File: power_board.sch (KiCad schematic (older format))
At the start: 25 parts, among them CON1 MICROUSB, J3 Conn_02x03_Odd_Even, J31 Conn_01x01, J32 Conn_01x01, J33 Conn_01x01, J34 Conn_01x01, SW1 SW_Push, U2 FT232RL, U4 ATMEGA328P-AU, U8 PCA9555PW, U9 PCA9555PW, Y1 Crystal

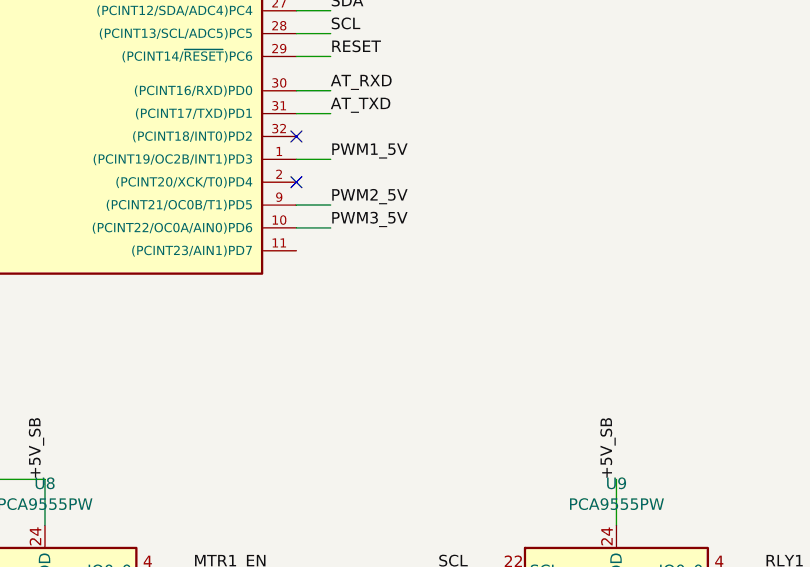
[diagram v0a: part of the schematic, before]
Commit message: Motor control positioning
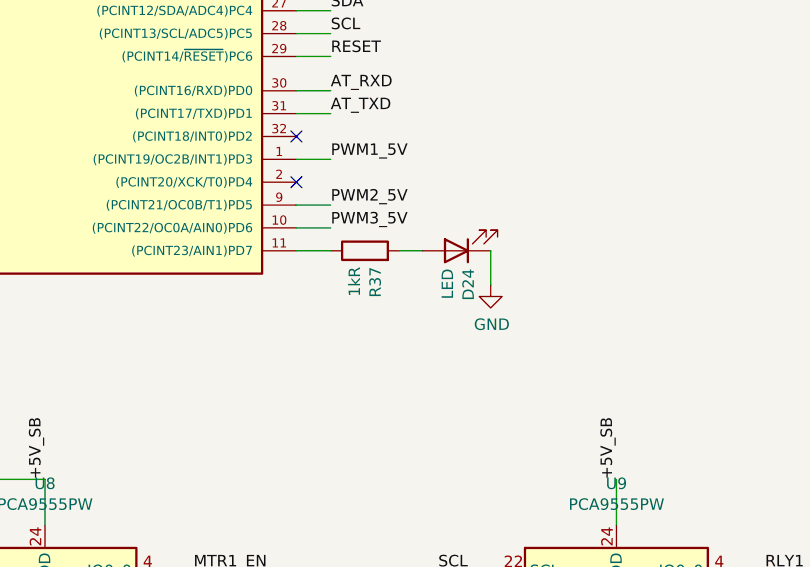
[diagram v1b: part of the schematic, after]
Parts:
- added D24: LED, lsts-discretes:LED_0603, symbol Device:LED
- added R37: 1kR, lsts-passives:R_0603, symbol Device:R
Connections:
- net GND: now also D24.1 (K)
- net at U4.11 ((PCINT23/AIN1)PD7): now also R37.1
- new net: D24.2 (A), R37.2
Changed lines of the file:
@@
 Text Label 3000 1500 0    50   ~ 0
 PWR_CTR
+$Comp
+L Device:LED D24
+U 1 1 5E321428
+P 3550 3800
+F 0 "D24" V 3497 3878 50  0000 L CNN
+F 1 "LED" V 3588 3878 50  0000 L CNN
+F 2 "lsts-discretes:LED_0603" H 3550 3800 50  0001 C CNN
+F 3 "~" H 3550 3800 50  0001 C CNN
+	1    3550 3800
+	-1   0    0    1
+$EndComp
+Wire Wire Line
+	3400 3800 3300 3800
+$Comp
+L Device:R R37
+U 1 1 5E32142F
+P 3150 3800
+F 0 "R37" H 3080 3754 50  0000 R CNN
+F 1 "1kR" H 3080 3845 50  0000 R CNN
+F 2 "lsts-passives:R_0603" V 3080 3800 50  0001 C CNN
+F 3 "~" H 3150 3800 50  0001 C CNN
+	1    3150 3800
+	0    -1   -1   0
+$EndComp
+Wire Wire Line
+	2850 3800 3000 3800
+$Comp
+L power:GND #PWR040
+U 1 1 5E35F179
+P 3700 3950
+F 0 "#PWR040" H 3700 3700 50  0001 C CNN
+F 1 "GND" H 3705 3777 50  0000 C CNN
+F 2 "" H 3700 3950 50  0001 C CNN
+F 3 "" H 3700 3950 50  0001 C CNN
+	1    3700 3950
+	1    0    0    -1
+$EndComp
+Wire Wire Line
+	3700 3800 3700 3950
 $EndSCHEMATC

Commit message: Motor control finished
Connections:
- net MTR6_BW: now also U9.6 (IO0_2)
- net MTR6_EN: now also U9.4 (IO0_0)
- net MTR6_FW: now also U9.5 (IO0_1)
- net MTR7_BW: now also U9.9 (IO0_5)
- net MTR7_EN: now also U9.7 (IO0_3)
- net MTR7_FW: now also U9.8 (IO0_4)
- net MTR8_BW: now also U9.13 (IO1_0)
- net MTR8_EN: now also U9.10 (IO0_6)
- net MTR8_FW: now also U9.11 (IO0_7)
- net RLY1_EN: now also U9.14 (IO1_1); no longer U9.4 (IO0_0)
- net RLY2_EN: now also U9.15 (IO1_2); no longer U9.5 (IO0_1)
- net RLY3_EN: now also U9.16 (IO1_3); no longer U9.6 (IO0_2)
- net RLY4_EN: now also U9.17 (IO1_4); no longer U9.7 (IO0_3)
- net RLY5_EN: now also U9.18 (IO1_5); no longer U9.8 (IO0_4)
- no-connect marks 34 -> 25
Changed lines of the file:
@@
 	2250 6700 2400 6700
 Wire Wire Line
-	4750 5200 4900 5200
-Wire Wire Line
-	4750 5300 4900 5300
-Wire Wire Line
-	4750 5400 4900 5400
-Wire Wire Line
-	4750 5500 4900 5500
-Wire Wire Line
-	4750 5600 4900 5600
+	4750 6200 4900 6200
+Wire Wire Line
+	4750 6300 4900 6300
+Wire Wire Line
+	4750 6400 4900 6400
+Wire Wire Line
+	4750 6500 4900 6500
+Wire Wire Line
+	4750 6600 4900 6600
 Text Label 2400 5200 0    50   ~ 0
 MTR1_EN
@@
 Text Label 2400 6700 0    50   ~ 0
 MTR5_BW
-Text Label 4900 5200 0    50   ~ 0
+Text Label 4900 6200 0    50   ~ 0
 RLY1_EN
-Text Label 4900 5300 0    50   ~ 0
+Text Label 4900 6300 0    50   ~ 0
 RLY2_EN
-Text Label 4900 5400 0    50   ~ 0
+Text Label 4900 6400 0    50   ~ 0
 RLY3_EN
-Text Label 4900 5500 0    50   ~ 0
+Text Label 4900 6500 0    50   ~ 0
 RLY4_EN
-Text Label 4900 5600 0    50   ~ 0
+Text Label 4900 6600 0    50   ~ 0
 RLY5_EN
 $Comp
@@
 NoConn ~ 1250 5500
 NoConn ~ 2250 6800
-NoConn ~ 4750 5700
-NoConn ~ 4750 5800
-NoConn ~ 4750 5900
-NoConn ~ 4750 6100
-NoConn ~ 4750 6200
-NoConn ~ 4750 6300
-NoConn ~ 4750 6500
-NoConn ~ 4750 6400
-NoConn ~ 4750 6600
-NoConn ~ 4750 6700
-NoConn ~ 4750 6800
 NoConn ~ 950  2950
 NoConn ~ 950  2850
@@
 Wire Wire Line
 	1250 6800 1250 7050
-$Comp
-L Interface_Expansion:PCA9555PW U9
-U 1 1 5E2959DE
-P 4250 6000
-F 0 "U9" H 4250 7181 50  0000 C CNN
-F 1 "PCA9555PW" H 4250 7090 50  0000 C CNN
-F 2 "Package_SO:TSSOP-24_4.4x7.8mm_P0.65mm" H 4250 6000 50  0001 C CNN
-F 3 "https://www.nxp.com/docs/en/data-sheet/PCA9555.pdf" H 4250 6000 50  0001 C CNN
-F 4 "PCA9555PW,118" H 4250 6000 50  0001 C CNN "manf#"
-	1    4250 6000
-	1    0    0    -1
-$EndComp
 $Sheet
 S 9950 4600 550  600
@@
 Text Label 3000 1700 0    50   ~ 0
 PWM5_5V
-Wire Wire Line
-	3750 6700 3750 6800
-Connection ~ 3750 6800
-Wire Wire Line
-	3750 6800 3750 7050
 NoConn ~ 2850 3300
 NoConn ~ 2850 3500
@@
 Wire Wire Line
 	3700 3800 3700 3950
+Wire Wire Line
+	3750 6800 3750 7050
+Wire Wire Line
+	3750 6700 3750 6800
+Connection ~ 3750 6800
+$Comp
+L Interface_Expansion:PCA9555PW U9
+U 1 1 5E2959DE
+P 4250 6000
+F 0 "U9" H 4250 7181 50  0000 C CNN
+F 1 "PCA9555PW" H 4250 7090 50  0000 C CNN
+F 2 "Package_SO:TSSOP-24_4.4x7.8mm_P0.65mm" H 4250 6000 50  0001 C CNN
+F 3 "https://www.nxp.com/docs/en/data-sheet/PCA9555.pdf" H 4250 6000 50  0001 C CNN
+F 4 "PCA9555PW,118" H 4250 6000 50  0001 C CNN "manf#"
+	1    4250 6000
+	1    0    0    -1
+$EndComp
+Wire Wire Line
+	4750 5200 4900 5200
+Wire Wire Line
+	4750 5300 4900 5300
+Wire Wire Line
+	4750 5400 4900 5400
+Text Label 4900 5200 0    50   ~ 0
+MTR6_EN
+Text Label 4900 5300 0    50   ~ 0
+MTR6_FW
+Text Label 4900 5400 0    50   ~ 0
+MTR6_BW
+Wire Wire Line
+	4750 5500 4900 5500
+Wire Wire Line
+	4750 5600 4900 5600
+Wire Wire Line
+	4750 5700 4900 5700
+Text Label 4900 5500 0    50   ~ 0
+MTR7_EN
+Text Label 4900 5600 0    50   ~ 0
+MTR7_FW
+Text Label 4900 5700 0    50   ~ 0
+MTR7_BW
+Wire Wire Line
+	4750 5800 4900 5800
+Wire Wire Line
+	4750 5900 4900 5900
+Wire Wire Line
+	4750 6100 4900 6100
+Text Label 4900 5800 0    50   ~ 0
+MTR8_EN
+Text Label 4900 5900 0    50   ~ 0
+MTR8_FW
+Text Label 4900 6100 0    50   ~ 0
+MTR8_BW
+NoConn ~ 4750 6700
+NoConn ~ 4750 6800
 $EndSCHEMATC

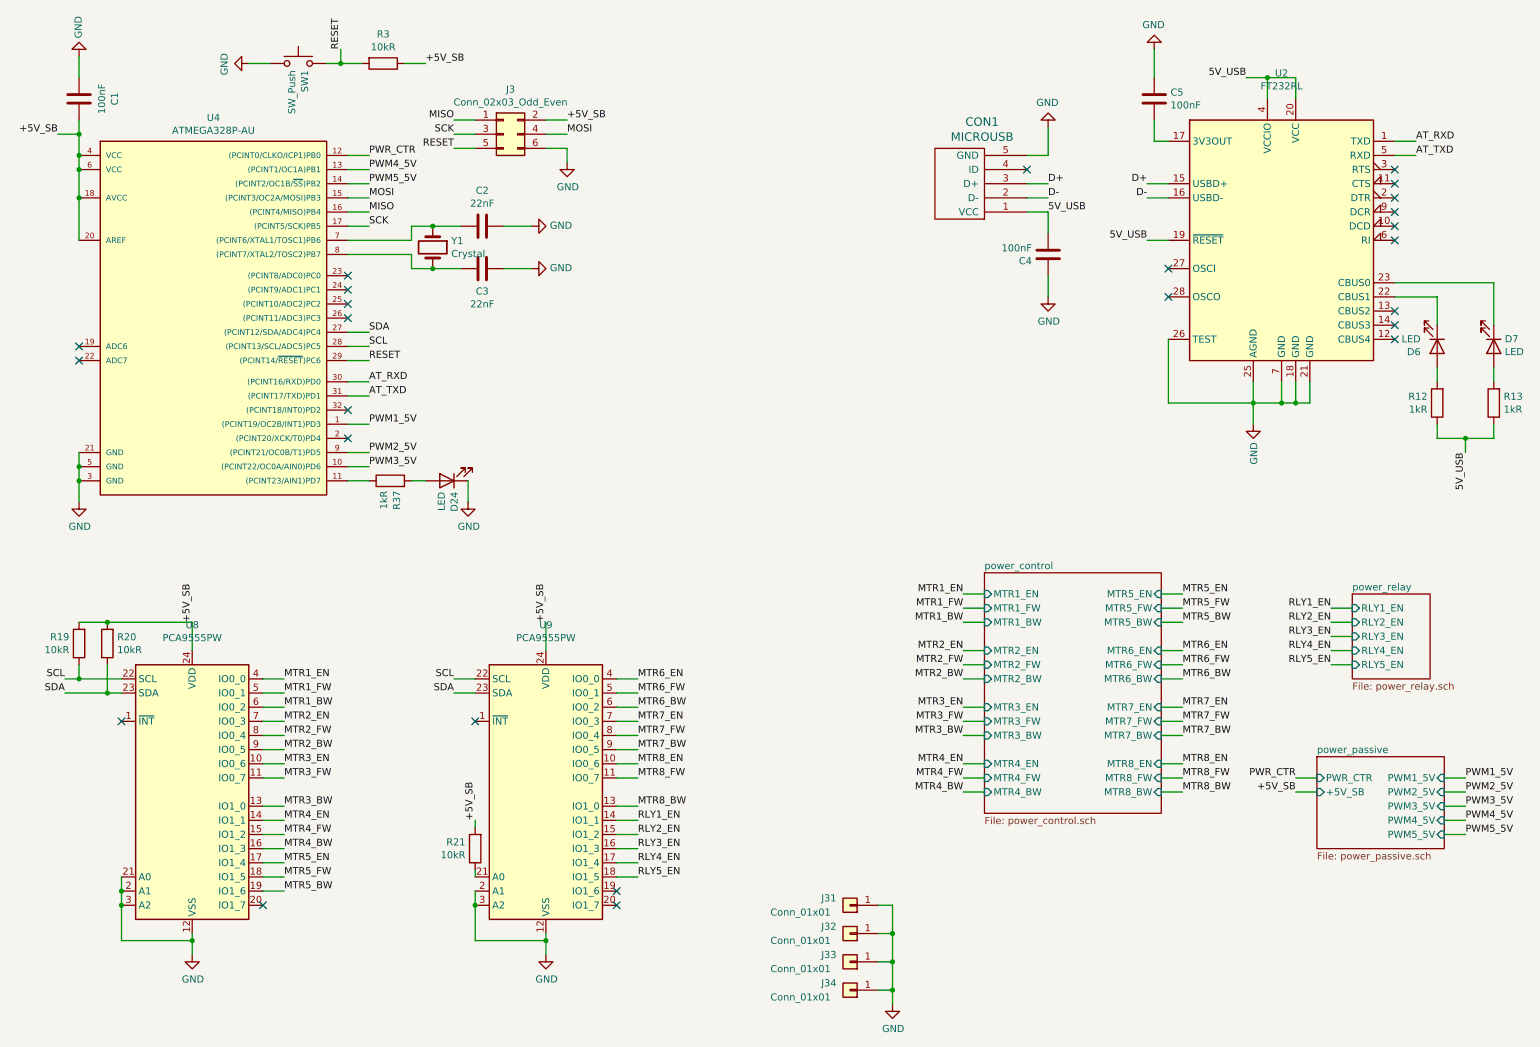
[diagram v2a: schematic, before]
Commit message: Positioning finished
Lacks fine alignment.
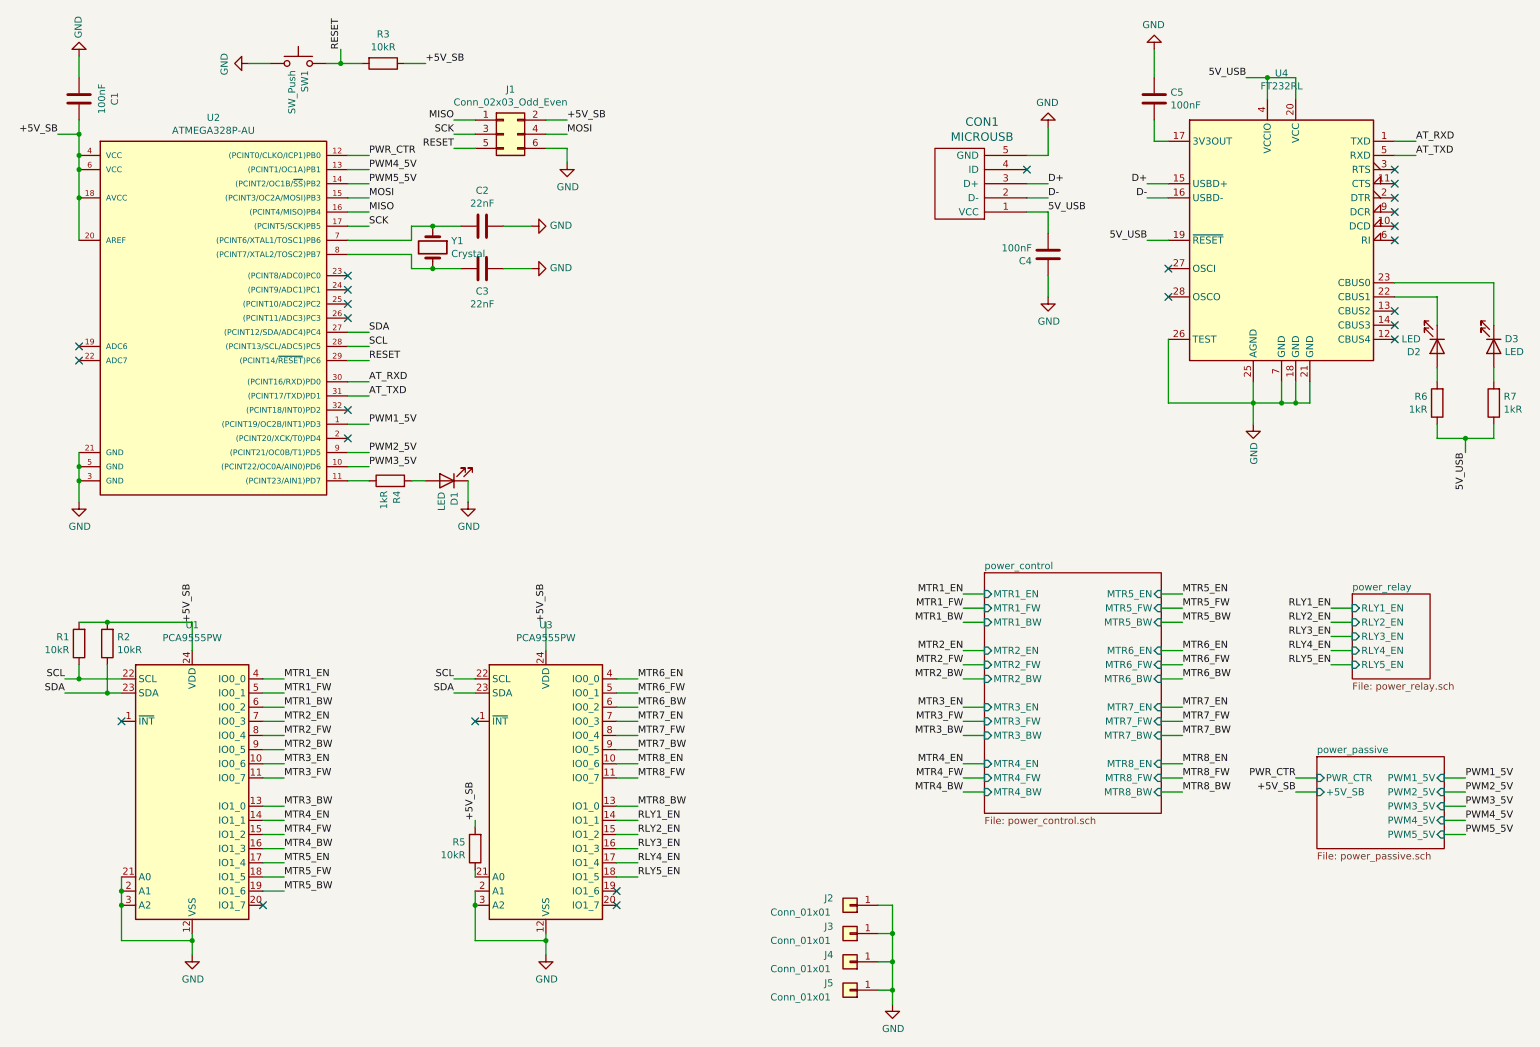
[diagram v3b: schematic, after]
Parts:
- renumbered D24 to D1, D6 to D2, D7 to D3, J3 to J1, J31 to J2, J32 to J3, J33 to J4, J34 to J5, R19 to R1, R20 to R2, R37 to R4, R21 to R5, R12 to R6, R13 to R7, U8 to U1, U4 to U2, U9 to U3, U2 to U4
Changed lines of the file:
@@
 $EndDescr
 $Comp
-L Interface_USB:FT232RL U2
+L Interface_USB:FT232RL U4
 U 1 1 5DC05EB6
 P 9450 2100
-F 0 "U2" H 9450 3281 50  0000 C CNN
+F 0 "U4" H 9450 3281 50  0000 C CNN
 F 1 "FT232RL" H 9450 3190 50  0000 C CNN
 F 2 "Package_SO:SSOP-28_5.3x10.2mm_P0.65mm" H 10550 1200 50  0001 C CNN
@@
 	9550 3250 9450 3250
 $Comp
-L power:GND #PWR0101
+L power:GND #PWR014
 U 1 1 5DC0D5DB
 P 9250 3400
-F 0 "#PWR0101" H 9250 3150 50  0001 C CNN
+F 0 "#PWR014" H 9250 3150 50  0001 C CNN
 F 1 "GND" V 9255 3272 50  0000 R CNN
 F 2 "" H 9250 3400 50  0001 C CNN
@@
 	7650 1900 7800 1900
 $Comp
-L power:GND #PWR0102
+L power:GND #PWR011
 U 1 1 5DC4811C
 P 7800 1300
-F 0 "#PWR0102" H 7800 1050 50  0001 C CNN
+F 0 "#PWR011" H 7800 1050 50  0001 C CNN
 F 1 "GND" H 7805 1127 50  0000 C CNN
 F 2 "" H 7800 1300 50  0001 C CNN
@@
 D+
 $Comp
-L Device:LED D6
+L Device:LED D2
 U 1 1 5DC5640F
 P 10550 2850
-F 0 "D6" V 10589 2733 50  0000 R CNN
+F 0 "D2" V 10589 2733 50  0000 R CNN
 F 1 "LED" V 10498 2733 50  0000 R CNN
 F 2 "lsts-discretes:LED_0603" H 10550 2850 50  0001 C CNN
@@
 $EndComp
 $Comp
-L Device:LED D7
+L Device:LED D3
 U 1 1 5DC512F1
 P 10950 2850
-F 0 "D7" V 10897 2928 50  0000 L CNN
+F 0 "D3" V 10897 2928 50  0000 L CNN
 F 1 "LED" V 10988 2928 50  0000 L CNN
 F 2 "lsts-discretes:LED_0603" H 10950 2850 50  0001 C CNN
@@
 	10550 3000 10550 3100
 $Comp
-L Device:R R12
+L Device:R R6
 U 1 1 5DC5D511
 P 10550 3250
-F 0 "R12" H 10619 3204 50  0000 L CNN
+F 0 "R6" H 10619 3204 50  0000 L CNN
 F 1 "1kR" H 10619 3295 50  0000 L CNN
 F 2 "lsts-passives:R_0603" V 10480 3250 50  0001 C CNN
@@
 $EndComp
 $Comp
-L Device:R R13
+L Device:R R7
 U 1 1 5DC5D870
 P 10950 3250
-F 0 "R13" H 10880 3204 50  0000 R CNN
+F 0 "R7" H 10880 3204 50  0000 R CNN
 F 1 "1kR" H 10880 3295 50  0000 R CNN
 F 2 "lsts-passives:R_0603" V 10880 3250 50  0001 C CNN
@@
 	10550 2500 10550 2700
 $Comp
-L Connector_Generic:Conn_02x03_Odd_Even J3
+L Connector_Generic:Conn_02x03_Odd_Even J1
 U 1 1 5DC8B0D2
 P 3950 1350
-F 0 "J3" H 4000 1667 50  0000 C CNN
+F 0 "J1" H 4000 1667 50  0000 C CNN
 F 1 "Conn_02x03_Odd_Even" H 4000 1576 50  0000 C CNN
 F 2 "lsts-conn:CONN_ISP" H 3950 1350 50  0001 C CNN
@@
 	3750 1450 3600 1450
 $Comp
-L power:GND #PWR0105
+L power:GND #PWR09
 U 1 1 5DC9272C
 P 4400 1550
-F 0 "#PWR0105" H 4400 1300 50  0001 C CNN
+F 0 "#PWR09" H 4400 1300 50  0001 C CNN
 F 1 "GND" H 4405 1377 50  0000 C CNN
 F 2 "" H 4400 1550 50  0001 C CNN
@@
 $EndComp
 $Comp
-L power:GND #PWR0106
+L power:GND #PWR012
 U 1 1 5DCA65D2
 P 7800 2500
-F 0 "#PWR0106" H 7800 2250 50  0001 C CNN
+F 0 "#PWR012" H 7800 2250 50  0001 C CNN
 F 1 "GND" H 7805 2327 50  0000 C CNN
 F 2 "" H 7800 2500 50  0001 C CNN
@@
 NoConn ~ 10250 2800
 $Comp
-L power:GND #PWR0107
+L power:GND #PWR02
 U 1 1 5DC3EC2B
 P 950 3950
-F 0 "#PWR0107" H 950 3700 50  0001 C CNN
+F 0 "#PWR02" H 950 3700 50  0001 C CNN
 F 1 "GND" H 955 3777 50  0000 C CNN
 F 2 "" H 950 3950 50  0001 C CNN
@@
 $EndComp
 $Comp
-L power:GND #PWR0109
+L power:GND #PWR01
 U 1 1 5DC4DED9
 P 950 800
-F 0 "#PWR0109" H 950 550 50  0001 C CNN
+F 0 "#PWR01" H 950 550 50  0001 C CNN
 F 1 "GND" V 955 672 50  0000 R CNN
 F 2 "" H 950 800 50  0001 C CNN
@@
 	2300 850  2150 850
 $Comp
-L power:GND #PWR0110
+L power:GND #PWR04
 U 1 1 5DC6E12C
 P 2150 850
-F 0 "#PWR0110" H 2150 600 50  0001 C CNN
+F 0 "#PWR04" H 2150 600 50  0001 C CNN
 F 1 "GND" H 2155 677 50  0000 C CNN
 F 2 "" H 2150 850 50  0001 C CNN
@@
 $EndComp
 $Comp
-L power:GND #PWR0111
+L power:GND #PWR06
 U 1 1 5DC9BC40
 P 4150 2000
-F 0 "#PWR0111" H 4150 1750 50  0001 C CNN
+F 0 "#PWR06" H 4150 1750 50  0001 C CNN
 F 1 "GND" V 4155 1872 50  0000 R CNN
 F 2 "" H 4150 2000 50  0001 C CNN
@@
 $EndComp
 $Comp
-L power:GND #PWR0112
+L power:GND #PWR07
 U 1 1 5DC9C15F
 P 4150 2300
-F 0 "#PWR0112" H 4150 2050 50  0001 C CNN
+F 0 "#PWR07" H 4150 2050 50  0001 C CNN
 F 1 "GND" V 4155 2172 50  0000 R CNN
 F 2 "" H 4150 2300 50  0001 C CNN
@@
 	1750 7050 1750 7150
 $Comp
-L power:GND #PWR0192
+L power:GND #PWR03
 U 1 1 5E1B9B28
 P 1750 7150
-F 0 "#PWR0192" H 1750 6900 50  0001 C CNN
+F 0 "#PWR03" H 1750 6900 50  0001 C CNN
 F 1 "GND" H 1755 6977 50  0000 C CNN
 F 2 "" H 1750 7150 50  0001 C CNN
@@
 	4250 7050 4250 7150
 $Comp
-L power:GND #PWR0193
+L power:GND #PWR08
 U 1 1 5E1C2465
 P 4250 7150
-F 0 "#PWR0193" H 4250 6900 50  0001 C CNN
+F 0 "#PWR08" H 4250 6900 50  0001 C CNN
 F 1 "GND" H 4255 6977 50  0000 C CNN
 F 2 "" H 4250 7150 50  0001 C CNN
@@
 RLY5_EN
 $Comp
-L Device:R R21
+L Device:R R5
 U 1 1 5E1910A1
 P 3750 6400
-F 0 "R21" H 3819 6354 50  0000 L CNN
+F 0 "R5" H 3819 6354 50  0000 L CNN
 F 1 "10kR" H 3819 6445 50  0000 L CNN
 F 2 "lsts-passives:R_0603" V 3680 6400 50  0001 C CNN
@@
 	3750 6200 3750 6250
 $Comp
-L Device:R R20
+L Device:R R2
 U 1 1 5E1C3EAF
 P 1150 4950
-F 0 "R20" H 1080 4904 50  0000 R CNN
+F 0 "R2" H 1080 4904 50  0000 R CNN
 F 1 "10kR" H 1080 4995 50  0000 R CNN
 F 2 "lsts-passives:R_0603" V 1080 4950 50  0001 C CNN
@@
 $EndComp
 $Comp
-L Device:R R19
+L Device:R R1
 U 1 1 5E1CDA66
 P 950 4950
-F 0 "R19" H 1019 4904 50  0000 L CNN
+F 0 "R1" H 1019 4904 50  0000 L CNN
 F 1 "10kR" H 1019 4995 50  0000 L CNN
 F 2 "lsts-passives:R_0603" V 880 4950 50  0001 C CNN
@@
 	9350 1100 9350 950
 $Comp
-L power:GND #PWR0103
+L power:GND #PWR013
 U 1 1 5DC6C013
 P 8550 750
-F 0 "#PWR0103" H 8550 500 50  0001 C CNN
+F 0 "#PWR013" H 8550 500 50  0001 C CNN
 F 1 "GND" H 8555 577 50  0000 C CNN
 F 2 "" H 8550 750 50  0001 C CNN
@@
 	4250 4800 4250 5000
 $Comp
-L Interface_Expansion:PCA9555PW U8
+L Interface_Expansion:PCA9555PW U1
 U 1 1 5E28C31F
 P 1750 6000
-F 0 "U8" H 1750 7181 50  0000 C CNN
+F 0 "U1" H 1750 7181 50  0000 C CNN
 F 1 "PCA9555PW" H 1750 7090 50  0000 C CNN
 F 2 "Package_SO:TSSOP-24_4.4x7.8mm_P0.65mm" H 1750 6000 50  0001 C CNN
@@
 NoConn ~ 2850 2350
 $Comp
-L Connector_Generic:Conn_01x01 J34
+L Connector_Generic:Conn_01x01 J5
 U 1 1 5E28827E
 P 6400 7400
-F 0 "J34" H 6550 7350 50  0000 C CNN
+F 0 "J5" H 6550 7350 50  0000 C CNN
 F 1 "Conn_01x01" H 6750 7450 50  0000 C CNN
 F 2 "lsts-mecanical:MountingHole_3.5mm_Pad" H 6400 7400 50  0001 C CNN
@@
 $EndComp
 $Comp
-L Connector_Generic:Conn_01x01 J33
+L Connector_Generic:Conn_01x01 J4
 U 1 1 5E28A83A
 P 6400 7200
-F 0 "J33" H 6550 7150 50  0000 C CNN
+F 0 "J4" H 6550 7150 50  0000 C CNN
 F 1 "Conn_01x01" H 6750 7250 50  0000 C CNN
 F 2 "lsts-mecanical:MountingHole_3.5mm_Pad" H 6400 7200 50  0001 C CNN
@@
 $EndComp
 $Comp
-L Connector_Generic:Conn_01x01 J32
+L Connector_Generic:Conn_01x01 J3
 U 1 1 5E29484D
 P 6400 7000
-F 0 "J32" H 6550 6950 50  0000 C CNN
+F 0 "J3" H 6550 6950 50  0000 C CNN
 F 1 "Conn_01x01" H 6750 7050 50  0000 C CNN
 F 2 "lsts-mecanical:MountingHole_3.5mm_Pad" H 6400 7000 50  0001 C CNN
@@
 $EndComp
 $Comp
-L Connector_Generic:Conn_01x01 J31
+L Connector_Generic:Conn_01x01 J2
 U 1 1 5E294857
 P 6400 6800
-F 0 "J31" H 6550 6750 50  0000 C CNN
+F 0 "J2" H 6550 6750 50  0000 C CNN
 F 1 "Conn_01x01" H 6750 6850 50  0000 C CNN
 F 2 "lsts-mecanical:MountingHole_3.5mm_Pad" H 6400 6800 50  0001 C CNN
@@
 $EndComp
 $Comp
-L power:GND #PWR038
+L power:GND #PWR010
 U 1 1 5E29E574
 P 6700 7500
-F 0 "#PWR038" H 6700 7250 50  0001 C CNN
+F 0 "#PWR010" H 6700 7250 50  0001 C CNN
 F 1 "GND" H 6705 7327 50  0000 C CNN
 F 2 "" H 6700 7500 50  0001 C CNN
@@
 Connection ~ 950  1800
 $Comp
-L lsts-micros:ATMEGA328P-AU U4
+L lsts-micros:ATMEGA328P-AU U2
 U 1 1 5DFA533E
 P 1850 2600
-F 0 "U4" H 1900 3967 50  0000 C CNN
+F 0 "U2" H 1900 3967 50  0000 C CNN
 F 1 "ATMEGA328P-AU" H 1900 3876 50  0000 C CNN
 F 2 "lsts-ic:TQFP32" H 1850 2600 50  0001 C CIN
@@
 PWR_CTR
 $Comp
-L Device:LED D24
+L Device:LED D1
 U 1 1 5E321428
 P 3550 3800
-F 0 "D24" V 3497 3878 50  0000 L CNN
+F 0 "D1" V 3497 3878 50  0000 L CNN
 F 1 "LED" V 3588 3878 50  0000 L CNN
 F 2 "lsts-discretes:LED_0603" H 3550 3800 50  0001 C CNN
@@
 	3400 3800 3300 3800
 $Comp
-L Device:R R37
+L Device:R R4
 U 1 1 5E32142F
 P 3150 3800
-F 0 "R37" H 3080 3754 50  0000 R CNN
+F 0 "R4" H 3080 3754 50  0000 R CNN
 F 1 "1kR" H 3080 3845 50  0000 R CNN
 F 2 "lsts-passives:R_0603" V 3080 3800 50  0001 C CNN
@@
 	2850 3800 3000 3800
 $Comp
-L power:GND #PWR040
+L power:GND #PWR05
 U 1 1 5E35F179
 P 3700 3950
-F 0 "#PWR040" H 3700 3700 50  0001 C CNN
+F 0 "#PWR05" H 3700 3700 50  0001 C CNN
 F 1 "GND" H 3705 3777 50  0000 C CNN
 F 2 "" H 3700 3950 50  0001 C CNN
@@
 Connection ~ 3750 6800
 $Comp
-L Interface_Expansion:PCA9555PW U9
+L Interface_Expansion:PCA9555PW U3
 U 1 1 5E2959DE
 P 4250 6000
-F 0 "U9" H 4250 7181 50  0000 C CNN
+F 0 "U3" H 4250 7181 50  0000 C CNN
 F 1 "PCA9555PW" H 4250 7090 50  0000 C CNN
 F 2 "Package_SO:TSSOP-24_4.4x7.8mm_P0.65mm" H 4250 6000 50  0001 C CNN
